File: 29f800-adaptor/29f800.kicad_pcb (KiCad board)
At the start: 2 copper layers, 9 parts, among them J1 Conn_01x02, J2 Conn_01x02, U1 27C400, U2 29F800

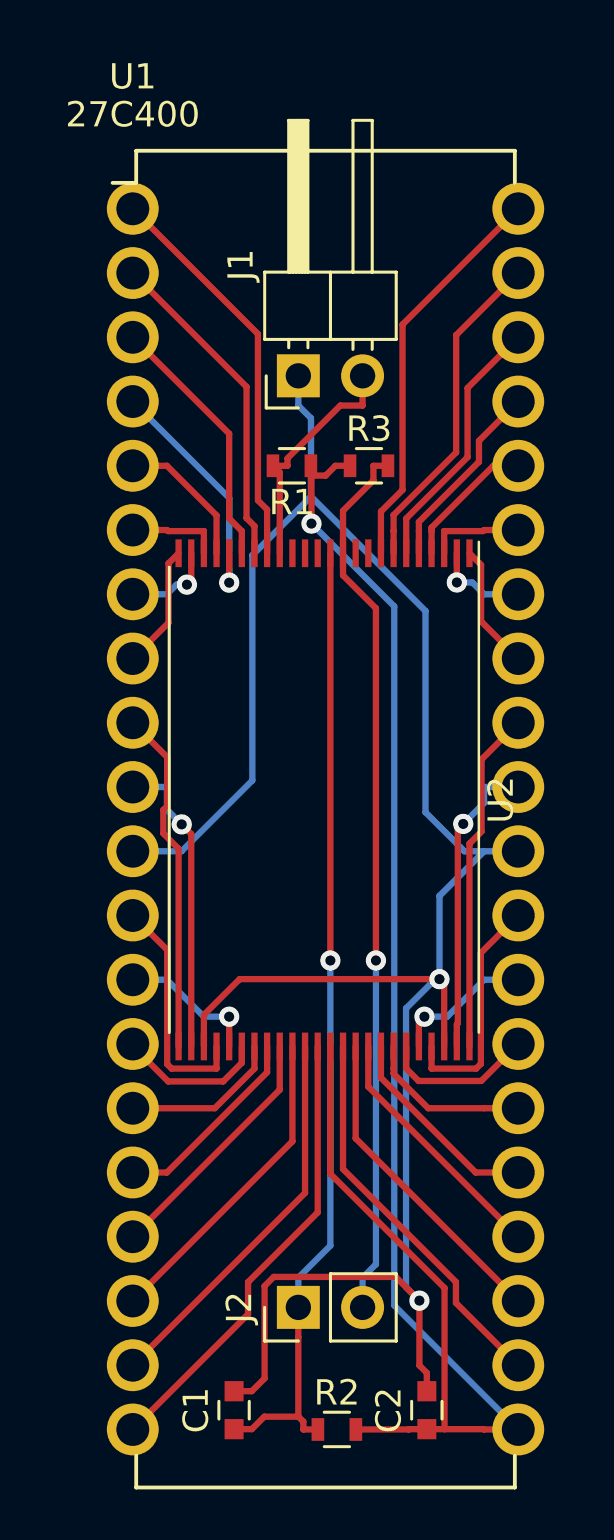
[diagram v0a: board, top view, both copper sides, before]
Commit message: KiCad 5 libs for 29f800 adapter
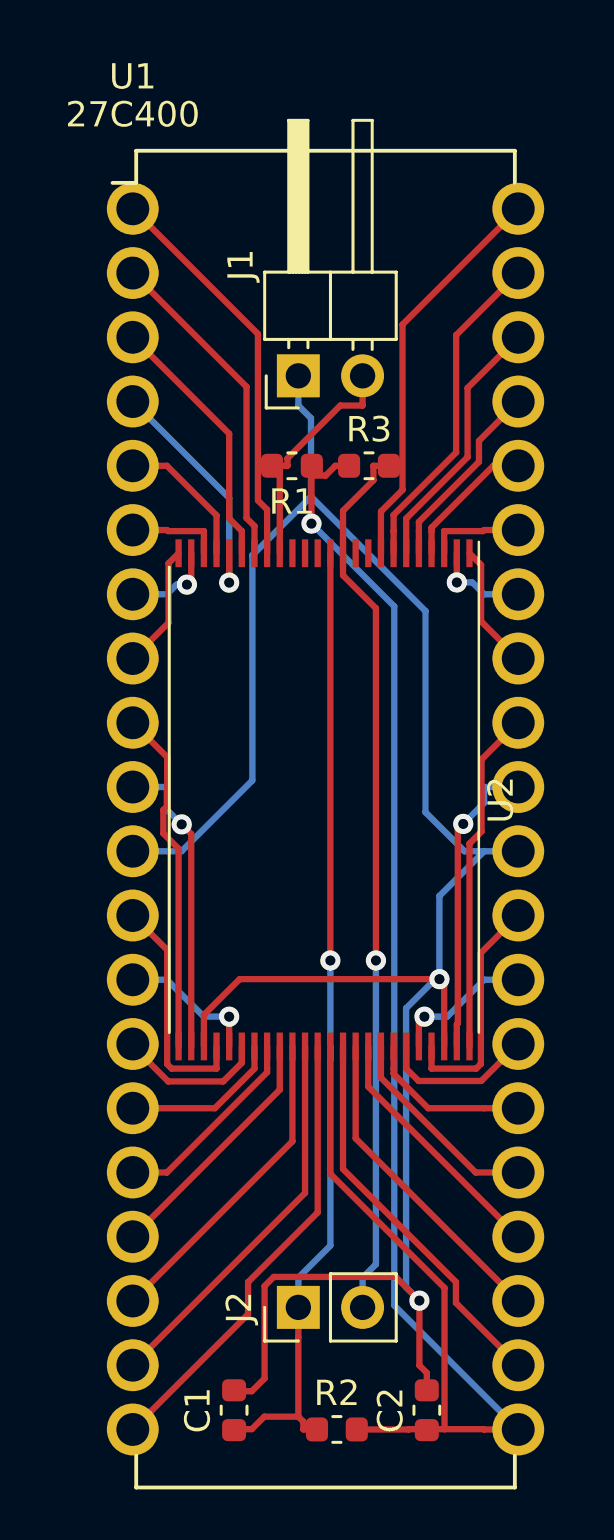
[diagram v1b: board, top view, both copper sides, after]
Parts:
- C1, C2: footprint Capacitors_SMD:C_0603 -> Capacitor_SMD:C_0603_1608Metric
- J1: footprint Pin_Headers:Pin_Header_Angled_1x02_Pitch2.54mm -> Connector_PinHeader_2.54mm:PinHeader_1x02_P2.54mm_Horizontal
- J2: footprint Pin_Headers:Pin_Header_Straight_1x02_Pitch2.54mm -> Connector_PinHeader_2.54mm:PinHeader_1x02_P2.54mm_Vertical
- R1, R2, R3: footprint Resistors_SMD:R_0603 -> Resistor_SMD:R_0603_1608Metric
- U2: footprint Housings_SSOP:TSOP-I-48_18.4x12mm_Pitch0.5mm -> Package_SO:TSOP-I-48_18.4x12mm_P0.5mm

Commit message: ReRouted after KiCad 5 libs because of bigger footprint
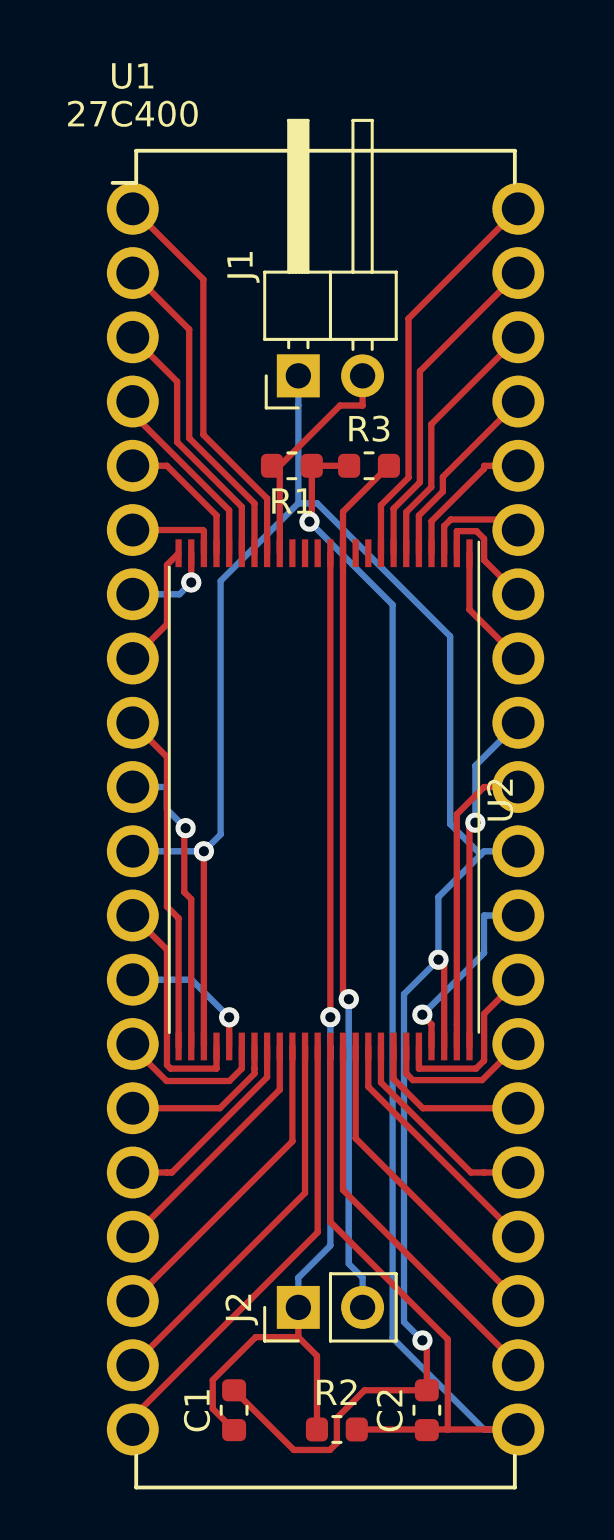
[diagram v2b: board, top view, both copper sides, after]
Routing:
- net VSS: track 90.4 -> 86.2 mm, vias 2 -> 3
- net /P_RST: track 38.6 -> 41.9 mm
- net /P4: track 9.90 -> 7.58 mm, vias 1 -> 0
- net /P28: track 5.58 -> 7.34 mm, vias 1 -> 0
- net /P29: track 9.38 -> 7.69 mm, vias 0 -> 1
- net /P34: track 3.78 -> 4.83 mm, vias 1 -> 0
- net /P_WE: track 35.1 -> 34.3 mm
- net VCC: track 66.6 -> 67.3 mm
- net /P32: vias 0 -> 1
- net /P31: vias 1 -> 0

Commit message: Added resistors and layout for A500 routing bug
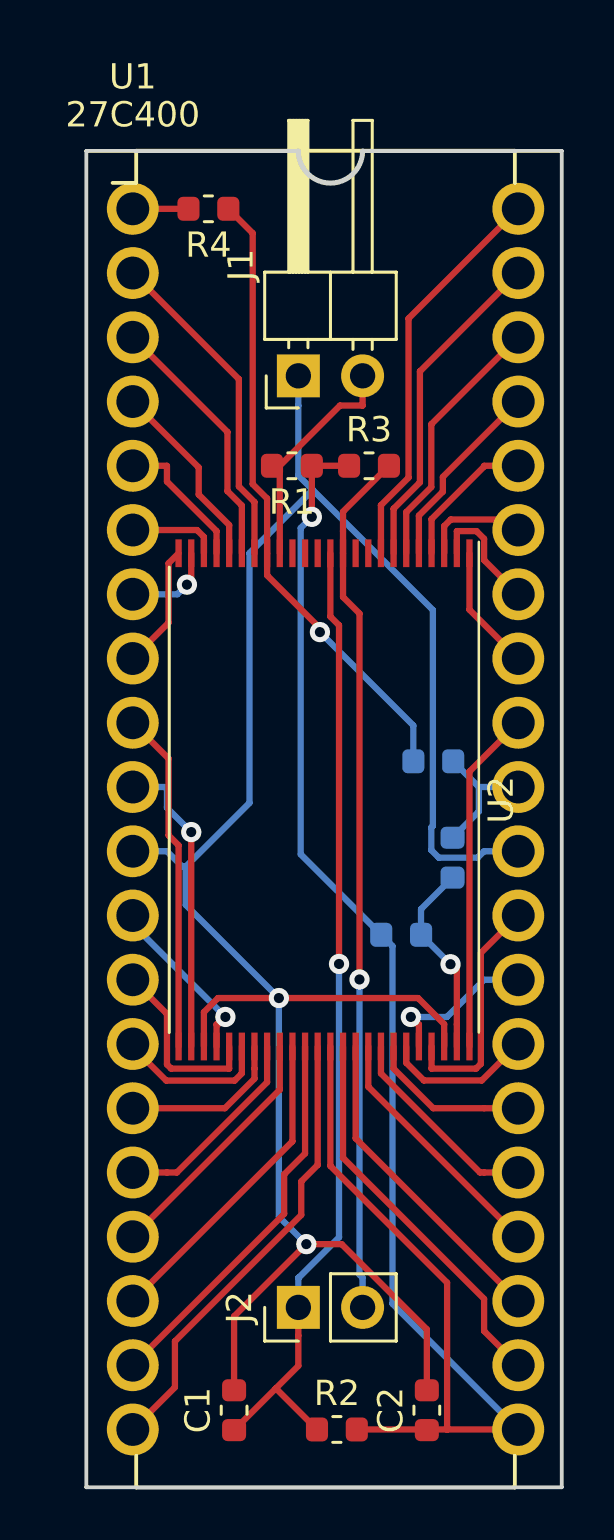
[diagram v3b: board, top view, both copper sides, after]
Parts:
- added R4: 0, Resistor_SMD:R_0603_1608Metric, F.Cu at (100.1, 63.8)
- added R5: 0, Resistor_SMD:R_0603_1608Metric, B.Cu at (109.7, 89.4)
- added R6: 0, Resistor_SMD:R_0603_1608Metric, B.Cu at (109.0, 85.6)
- added R7: 10k, Resistor_SMD:R_0603_1608Metric, B.Cu at (107.7, 92.5)
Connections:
- U1 pad 1: /P1 -> /P1_1
- U1 pad 31: /P31 -> /P31_1
- U2 pad 17: /P1 -> /P1_2
- U2 pad 47: /P31 -> /P31_2
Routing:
- net /P1_2: track 0.00 -> 24.9 mm, vias 0 -> 1
- net /P1: track 15.8 -> 0.00 mm
- net /P31: track 12.1 -> 0.00 mm
- net /P31_2: track 0.00 -> 7.78 mm, vias 0 -> 1
- net /P31_1: track 0.00 -> 5.43 mm
- net /P_RST: track 41.9 -> 38.8 mm
- net VSS: track 86.2 -> 88.8 mm, vias 3 -> 2
- net /P12: track 9.37 -> 6.87 mm, vias 0 -> 1
- net /P1_1: track 0.00 -> 2.20 mm
- net /P13: track 5.58 -> 7.31 mm, vias 1 -> 0
- net /P29: track 7.69 -> 9.38 mm, vias 1 -> 0
- net /P28: track 7.34 -> 6.17 mm, vias 0 -> 1
- net VCC: track 67.3 -> 66.8 mm
- net /P32: vias 1 -> 0
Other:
- board outline added: 18.8 x 52.8 mm
